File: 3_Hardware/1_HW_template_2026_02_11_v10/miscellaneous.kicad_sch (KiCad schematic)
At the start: 15 parts, among them Q1 BSS316N, SW1 ${SIM.PARAMS}, Y2 ${SIM.PARAMS}

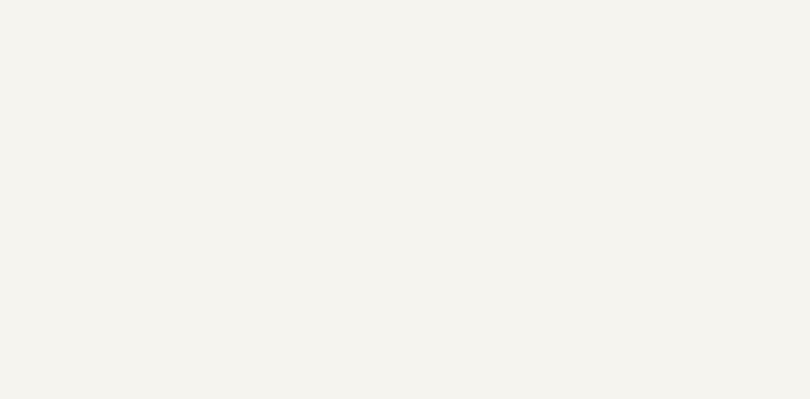
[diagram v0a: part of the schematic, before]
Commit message: first analog circuitry implemented in kicad
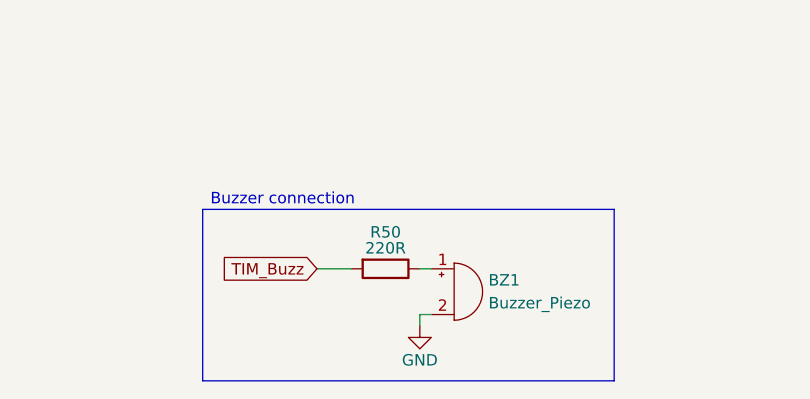
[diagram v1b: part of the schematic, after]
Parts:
- added BZ1: Buzzer_Piezo, Buzzer_Beeper:Buzzer_Murata_PKMCS0909E, symbol Device:Buzzer
- added R50: 220R, Resistor_SMD:R_0805_2012Metric_Pad1.20x1.40mm_HandSolder, symbol Device:R
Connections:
- net GND: now also BZ1.2 (-)
- new net: BZ1.1 (+), R50.1
- new net TIM_Buzz: R50.2
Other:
- note added: "Buzzer connection"

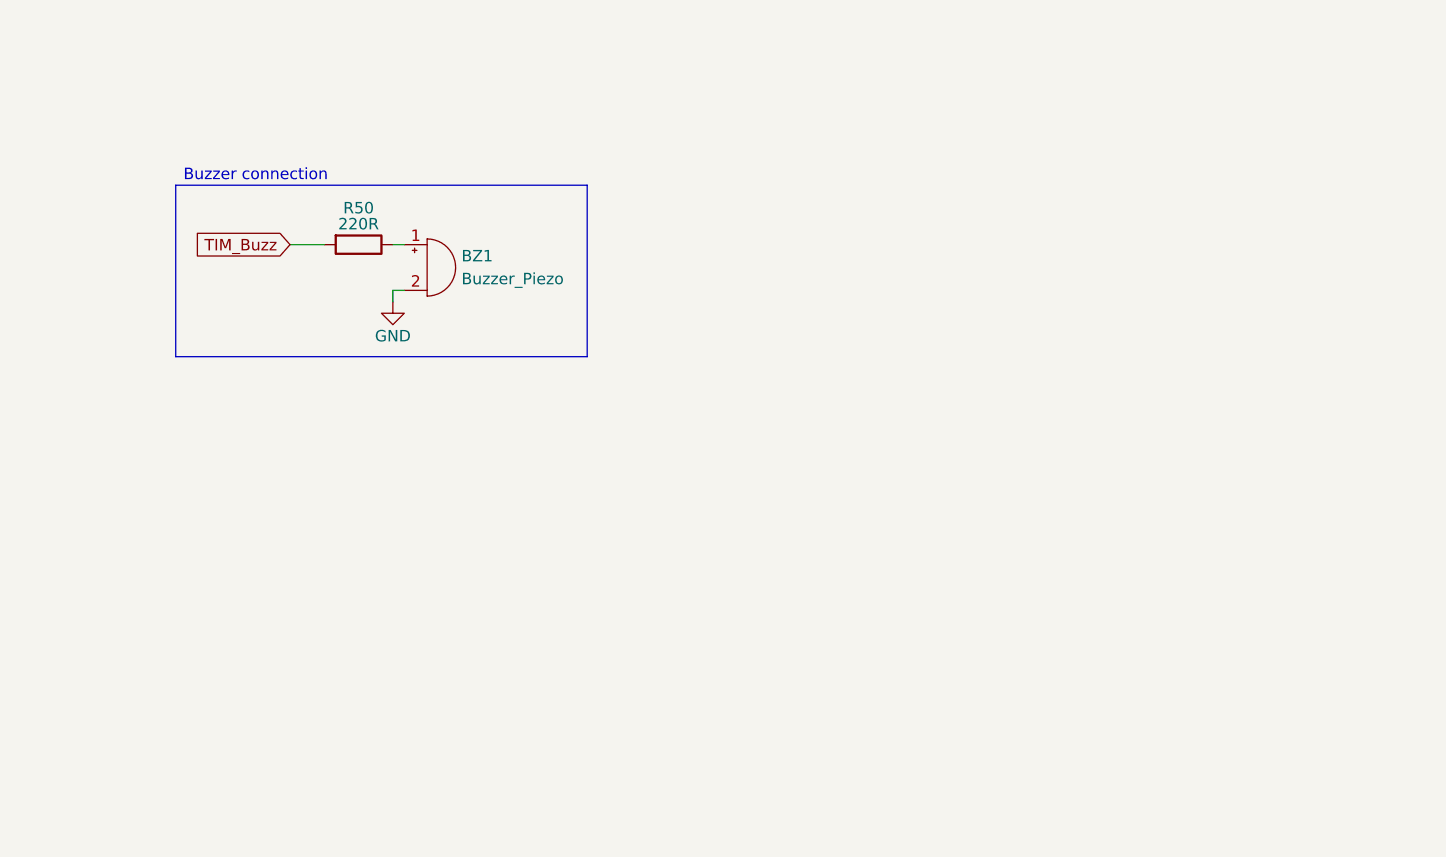
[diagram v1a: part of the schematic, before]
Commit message: finalize main feature
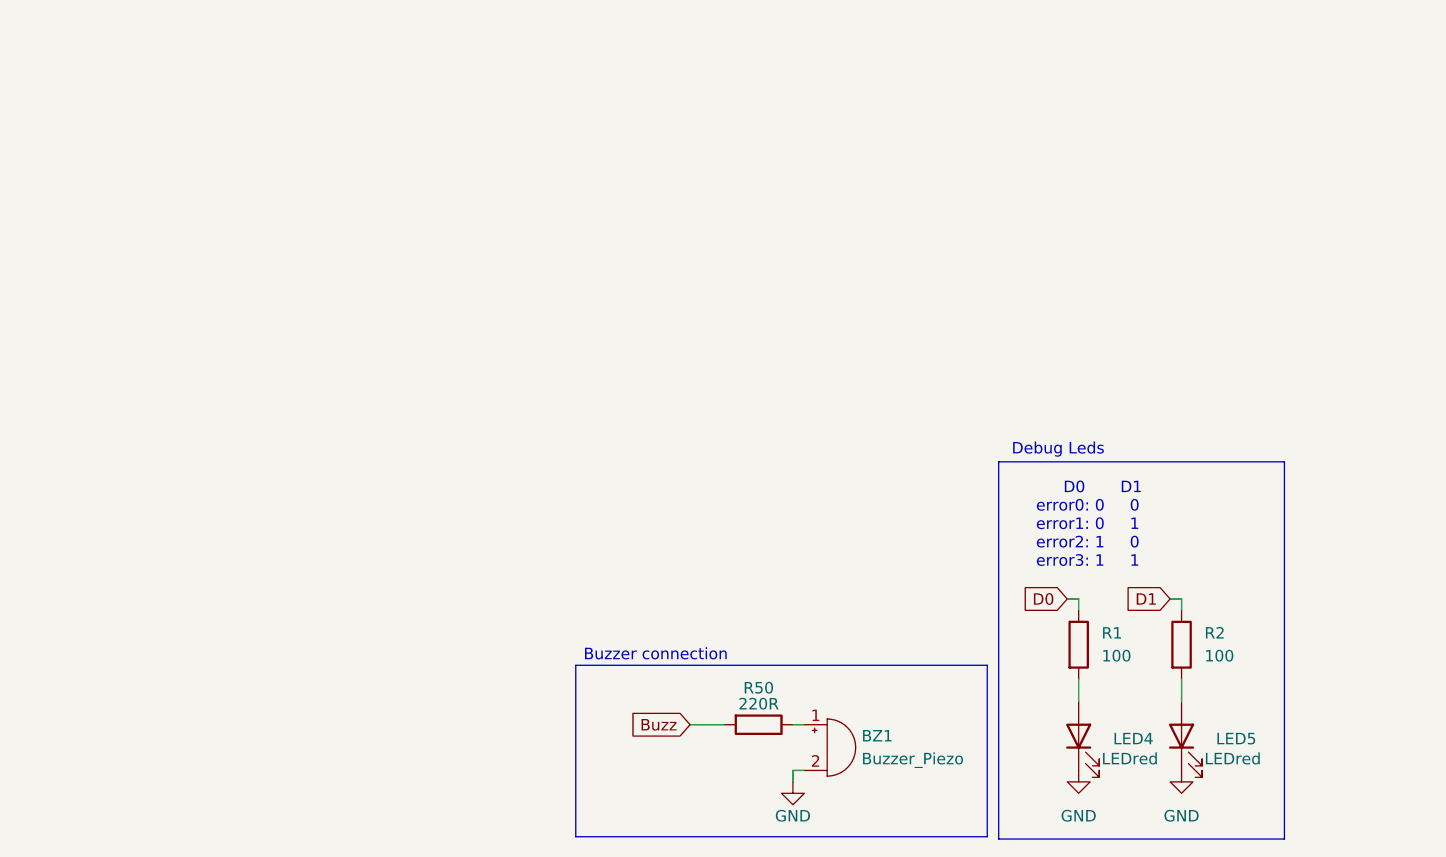
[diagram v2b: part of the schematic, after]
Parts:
- added LED4, LED5: LEDred, LED_SMD:LED_1206_3216Metric_Pad1.42x1.75mm_HandSolder, symbol Device:LED
- added R1, R2: 100, Resistor_SMD:R_0805_2012Metric_Pad1.20x1.40mm_HandSolder, symbol Device:R
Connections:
- net GND: now also LED4.1 (K), LED5.1 (K)
- net TIM_Buzz renamed Buzz
- new net: LED4.2 (A), R1.2
- new net: LED5.2 (A), R2.2
- new net D0: R1.1
- new net D1: R2.1
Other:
- note added: "D0 D1 error0: 0 0 error1: 0 1 error2: 1 0 error3: 1 1"
- note added: "Debug Leds"
- moved on the sheet: BZ1, R50

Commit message: layout template
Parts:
- removed LED1: LEDblue, LED_SMD:LED_1206_3216Metric_Pad1.42x1.75mm_HandSolder, symbol Device:LED
- removed LED2: LEDgreen, LED_SMD:LED_1206_3216Metric_Pad1.42x1.75mm_HandSolder, symbol Device:LED
- removed LED3: LEDred, LED_SMD:LED_1206_3216Metric_Pad1.42x1.75mm_HandSolder, symbol Device:LED
- removed Q1: BSS316N, Package_TO_SOT_SMD:SOT-23, symbol Transistor_FET:BSS138
- removed R16: 22, Resistor_SMD:R_0805_2012Metric_Pad1.20x1.40mm_HandSolder, symbol Device:R
- removed R17: 47, Resistor_SMD:R_0805_2012Metric_Pad1.20x1.40mm_HandSolder, symbol Device:R
- removed R18, R19, R20: 100, Resistor_SMD:R_0805_2012Metric_Pad1.20x1.40mm_HandSolder, symbol Device:R
- removed R21: 10, Resistor_SMD:R_0805_2012Metric_Pad1.20x1.40mm_HandSolder, symbol Device:R
- removed R22: 100k, Resistor_SMD:R_0805_2012Metric_Pad1.20x1.40mm_HandSolder, symbol Device:R
- removed SD1: SD103AWS, Diode_SMD:D_SOD-323_HandSoldering, symbol Device:D_Schottky
- removed SD2: SS13L, Diode_SMD:D_SMA, symbol Device:D_Schottky
- removed SW1: ${SIM.PARAMS}, Button_Switch_SMD:SW_SPST_PTS645, symbol Switch:SW_Push
- LED1: renamed from LED4; footprint LED_SMD:LED_1206_3216Metric_Pad1.42x1.75mm_HandSolder -> LED_SMD:LED_0603_1608Metric_Pad1.05x0.95mm_HandSolder
- LED2: renamed from LED5; footprint LED_SMD:LED_1206_3216Metric_Pad1.42x1.75mm_HandSolder -> LED_SMD:LED_0603_1608Metric_Pad1.05x0.95mm_HandSolder
- R16: renamed from R1; value 100 -> 1k; footprint Resistor_SMD:R_0805_2012Metric_Pad1.20x1.40mm_HandSolder -> Resistor_SMD:R_0603_1608Metric_Pad0.98x0.95mm_HandSolder
- R17: renamed from R2; value 100 -> 1k; footprint Resistor_SMD:R_0805_2012Metric_Pad1.20x1.40mm_HandSolder -> Resistor_SMD:R_0603_1608Metric_Pad0.98x0.95mm_HandSolder
- renumbered R50 to R15, Y2 to Y1
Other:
- note added: "Buzzer"
- note added: "D0 D1"
- note added: "The OpenLog extension"
- note added: "error0: 0 0 error1: 0 1 error2: 1 0 error3: 1 1"
- note removed: "Buzzer connection"
- note removed: "D0 D1 error0: 0 0 error1: 0 1 error2: 1 0 error3: 1 1"
- note removed: "LEDs with different colours"
- note removed: "MOSFET for load switching e.g. buzzer or power LED"
- note removed: "Miscellanneous components and subcircuits: Delete what is no used and copy components that are used several times."
- note removed: "Power Schottky"
- note removed: "Signal Schottky"
- note removed: "The OpenLog extension can be used for logging data onto an SD card"
- moved on the sheet: Y1

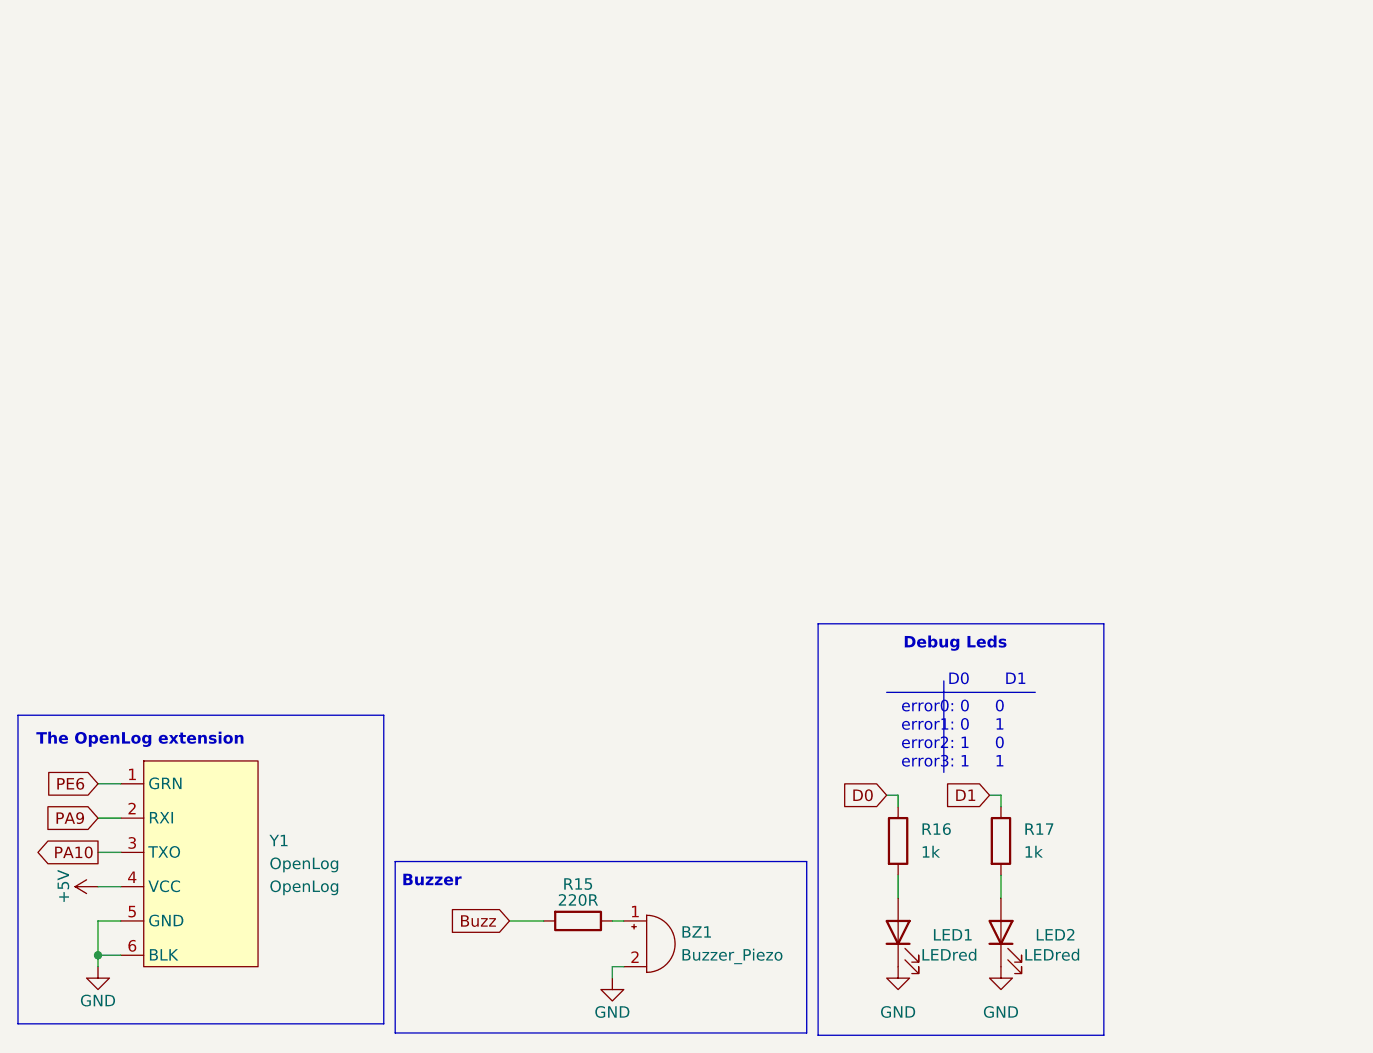
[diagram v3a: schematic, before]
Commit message: updated layout
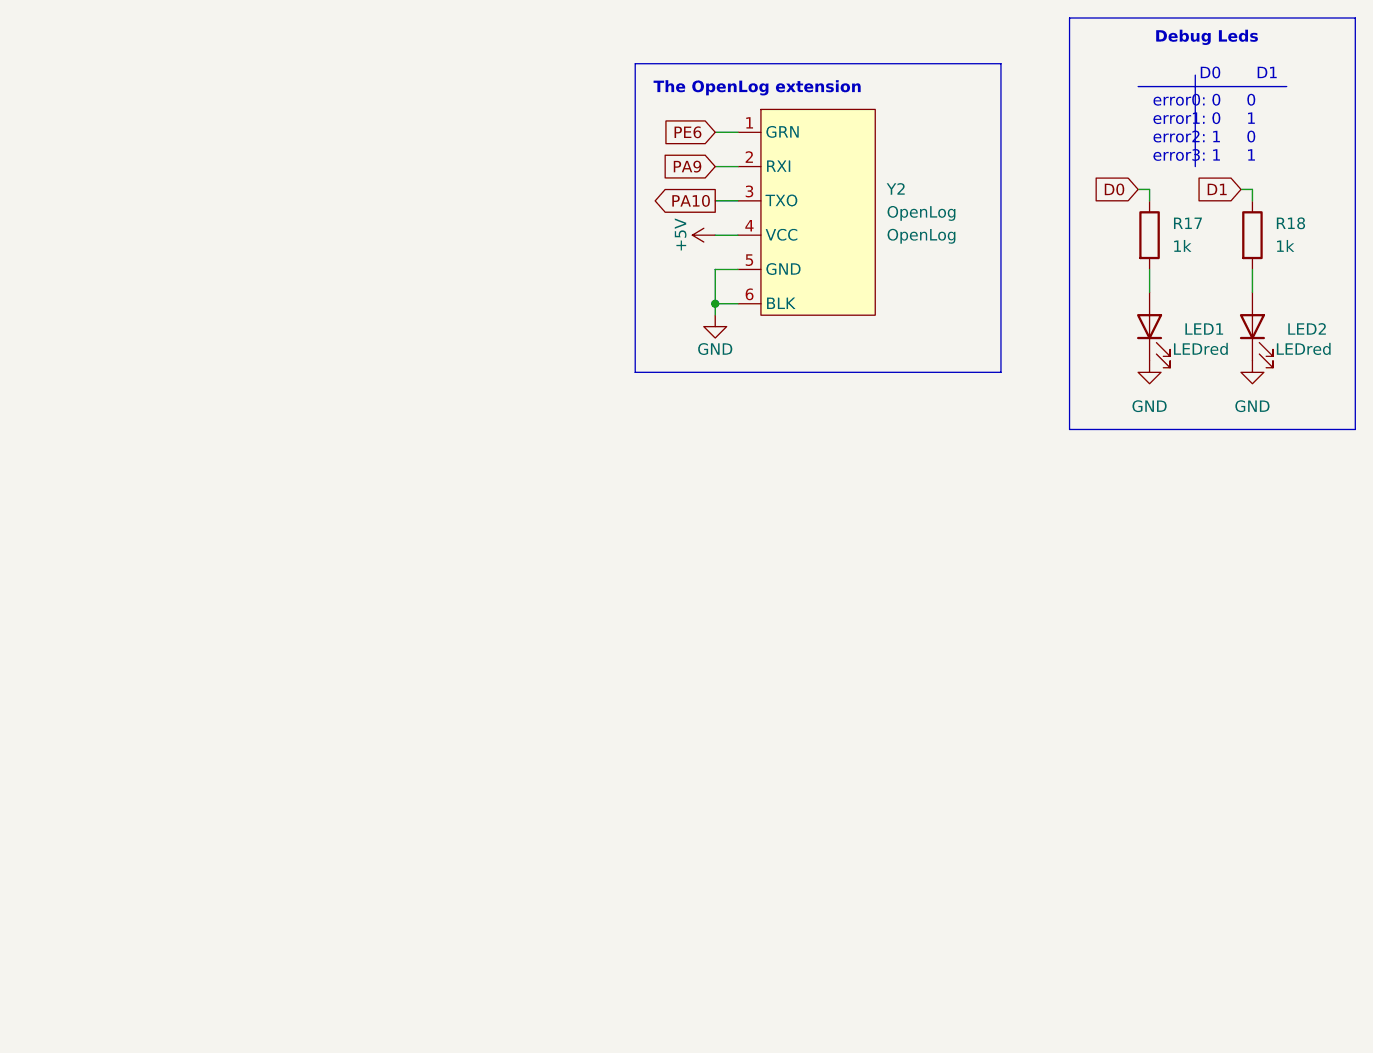
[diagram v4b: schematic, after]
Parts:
- removed BZ1: Buzzer_Piezo, Buzzer_Beeper:Buzzer_Murata_PKMCS0909E, symbol Device:Buzzer
- removed R15: 220R, Resistor_SMD:R_0805_2012Metric_Pad1.20x1.40mm_HandSolder, symbol Device:R
- renumbered R16 to R17, R17 to R18, Y1 to Y2
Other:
- note removed: "Buzzer"
- moved on the sheet: LED1, LED2, R17, R18, Y2

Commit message: pcb schematics finished + layout
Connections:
- net D0 renamed PE5
- net D1 renamed PE3
- net PA10: no longer names the net of Y2.3 (TXO)
- net PA9 renamed PG14_
- net PE6: no longer names the net of Y2.1 (GRN)
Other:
- moved on the sheet: Y2
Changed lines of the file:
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@@
 	(text "The OpenLog extension\n"
 		(exclude_from_sim no)
-		(at 125.222 92.456 0)
+		(at 127.762 92.456 0)
 		(effects
 			(font
@@
 	)
 	(junction
-		(at 132.08 115.57)
+		(at 134.62 115.57)
 		(diameter 0)
 		(color 0 0 0 0)
@@
 	(wire
 		(pts
-			(xy 132.08 111.76) (xy 132.08 115.57)
+			(xy 134.62 111.76) (xy 134.62 115.57)
 		)
 		(stroke
@@
 		)
 	)
-	(wire
-		(pts
-			(xy 132.08 96.52) (xy 134.62 96.52)
-		)
-		(stroke
-			(width 0)
-			(type default)
-		)
-	)
-	(wire
-		(pts
-			(xy 132.08 104.14) (xy 134.62 104.14)
-		)
-		(stroke
-			(width 0)
-			(type default)
-		)
-	)
 	(polyline
 		(pts
@@
 	(wire
 		(pts
-			(xy 132.08 107.95) (xy 134.62 107.95)
+			(xy 134.62 107.95) (xy 137.16 107.95)
 		)
 		(stroke
@@
 	(wire
 		(pts
-			(xy 132.08 115.57) (xy 132.08 116.84)
-		)
-		(stroke
-			(width 0)
-			(type default)
-		)
-	)
-	(wire
-		(pts
-			(xy 134.62 111.76) (xy 132.08 111.76)
-		)
-		(stroke
-			(width 0)
-			(type default)
-		)
-	)
-	(wire
-		(pts
-			(xy 132.08 100.33) (xy 134.62 100.33)
-		)
-		(stroke
-			(width 0)
-			(type default)
-		)
-	)
-	(wire
-		(pts
-			(xy 132.08 115.57) (xy 134.62 115.57)
+			(xy 134.62 115.57) (xy 134.62 116.84)
+		)
+		(stroke
+			(width 0)
+			(type default)
+		)
+	)
+	(wire
+		(pts
+			(xy 137.16 111.76) (xy 134.62 111.76)
+		)
+		(stroke
+			(width 0)
+			(type default)
+		)
+	)
+	(wire
+		(pts
+			(xy 134.62 100.33) (xy 137.16 100.33)
+		)
+		(stroke
+			(width 0)
+			(type default)
+		)
+	)
+	(wire
+		(pts
+			(xy 134.62 115.57) (xy 137.16 115.57)
 		)
 		(stroke
@@
 		)
 	)
-	(global_label "PA9"
+	(global_label "PG14_"
 		(shape input)
-		(at 132.08 100.33 180)
+		(at 134.62 100.33 180)
 		(fields_autoplaced yes)
 		(effects
@@
 		)
 		(property "Intersheetrefs" "${INTERSHEET_REFS}"
-			(at 126.0988 100.2506 0)
+			(at 125.7082 100.33 0)
 			(effects
 				(font
@@
 		)
 	)
-	(global_label "D1"
+	(global_label "PE3"
 		(shape input)
 		(at 190.5 102.87 180)
@@
 		)
 		(property "Intersheetrefs" "${INTERSHEET_REFS}"
-			(at 185.0353 102.87 0)
+			(at 183.8863 102.87 0)
 			(effects
 				(font
@@
 		)
 	)
-	(global_label "PE6"
-		(shape input)
-		(at 132.08 96.52 180)
-		(fields_autoplaced yes)
-		(effects
-			(font
-				(size 1.27 1.27)
-			)
-			(justify right)
-		)
-		(property "Intersheetrefs" "${INTERSHEET_REFS}"
-			(at 126.0383 96.4406 0)
-			(effects
-				(font
-					(size 1.27 1.27)
-				)
-				(justify right)
-				(hide yes)
-			)
-		)
-	)
-	(global_label "D0"
+	(global_label "PE5"
 		(shape input)
 		(at 179.07 102.87 180)
@@
 		)
 		(property "Intersheetrefs" "${INTERSHEET_REFS}"
-			(at 173.6053 102.87 0)
-			(effects
-				(font
-					(size 1.27 1.27)
-				)
-				(justify right)
-				(hide yes)
-			)
-		)
-	)
-	(global_label "PA10"
-		(shape output)
-		(at 132.08 104.14 180)
-		(fields_autoplaced yes)
-		(effects
-			(font
-				(size 1.27 1.27)
-			)
-			(justify right)
-		)
-		(property "Intersheetrefs" "${INTERSHEET_REFS}"
-			(at 124.8893 104.0606 0)
+			(at 172.4563 102.87 0)
 			(effects
 				(font
@@
 	(symbol
 		(lib_id "power:GND")
-		(at 132.08 116.84 0)
+		(at 134.62 116.84 0)
 		(unit 1)
 		(exclude_from_sim no)
@@
 		(dnp no)
 		(property "Reference" "#PWR027"
-			(at 132.08 123.19 0)
+			(at 134.62 123.19 0)
 			(effects
 				(font
@@
 		)
 		(property "Value" "GND"
-			(at 132.08 120.65 0)
+			(at 134.62 120.65 0)
 			(effects
 				(font
@@
 		)
 		(property "Footprint" ""
-			(at 132.08 116.84 0)
+			(at 134.62 116.84 0)
 			(effects
 				(font
@@
 		)
 		(property "Datasheet" ""
-			(at 132.08 116.84 0)
+			(at 134.62 116.84 0)
 			(effects
 				(font
@@
 		)
 		(property "Description" "Power symbol creates a global label with name \"GND\" , ground"
-			(at 132.08 116.84 0)
+			(at 134.62 116.84 0)
 			(effects
 				(font
@@
 	(symbol
 		(lib_id "HW_template:OpenLog")
-		(at 143.51 105.41 0)
+		(at 146.05 105.41 0)
 		(unit 1)
 		(exclude_from_sim no)
@@
 		(on_board yes)
 		(dnp no)
-		(fields_autoplaced yes)
 		(property "Reference" "Y2"
-			(at 151.13 102.8699 0)
+			(at 153.67 102.8699 0)
 			(effects
 				(font
@@
 		)
 		(property "Value" "${SIM.PARAMS}"
-			(at 151.13 105.4099 0)
+			(at 153.67 105.4099 0)
 			(effects
 				(font
@@
 		)
 		(property "Footprint" "Connector_PinHeader_2.54mm:PinHeader_1x06_P2.54mm_Vertical"
-			(at 147.32 120.65 0)
+			(at 149.86 120.65 0)
 			(effects
 				(font
@@
 		)
 		(property "Datasheet" "https://learn.sparkfun.com/tutorials/openlog-hookup-guide"
-			(at 144.78 123.19 0)
+			(at 147.32 123.19 0)
 			(effects
 				(font
@@
 		)
 		(property "Description" "extension for logging data onto an SD card"
-			(at 143.51 105.41 0)
+			(at 146.05 105.41 0)
 			(effects
 				(font
@@
 		)
 		(property "Sim.Device" "SPICE"
-			(at 143.51 105.41 0)
+			(at 146.05 105.41 0)
 			(effects
 				(font
@@
 		)
 		(property "Sim.Params" "OpenLog"
-			(at 151.13 107.9499 0)
+			(at 153.67 107.9499 0)
 			(effects
 				(font
@@
 				)
 				(justify left)
+				(hide yes)
 			)
 		)
 		(property "Sim.Pins" "1=1 2=2 3=3 4=4 5=5 6=6"
-			(at 143.51 105.41 0)
+			(at 146.05 105.41 0)
 			(effects
 				(font
@@
 	(symbol
 		(lib_id "power:+5V")
-		(at 132.08 107.95 90)
+		(at 134.62 107.95 90)
 		(unit 1)
 		(exclude_from_sim no)
@@
 		(dnp no)
 		(property "Reference" "#PWR026"
-			(at 135.89 107.95 0)
+			(at 138.43 107.95 0)
 			(effects
 				(font
@@
 		)
 		(property "Value" "+5V"
-			(at 128.27 107.95 0)
+			(at 130.81 107.95 0)
 			(effects
 				(font
@@
 		)
 		(property "Footprint" ""
-			(at 132.08 107.95 0)
+			(at 134.62 107.95 0)
 			(effects
 				(font
@@
 		)
 		(property "Datasheet" ""
-			(at 132.08 107.95 0)
+			(at 134.62 107.95 0)
 			(effects
 				(font
@@
 		)
 		(property "Description" "Power symbol creates a global label with name \"+5V\""
-			(at 132.08 107.95 0)
-			(effects
-				(font
+			(at 134.62 107.95 0)
+			(effects
+				(font

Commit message: finalized pcb
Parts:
- Y2: footprint Connector_PinHeader_2.54mm:PinHeader_1x06_P2.54mm_Vertical -> Connector_PinSocket_2.54mm:PinSocket_1x06_P2.54mm_Vertical
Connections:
- no-connect marks 0 -> 2
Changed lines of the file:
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@@
 		(color 0 0 0 0)
+	)
+	(no_connect
+		(at 137.16 96.52)
+	)
+	(no_connect
+		(at 137.16 104.14)
 	)
 	(wire
@@
 			)
 		)
-		(property "Footprint" "Connector_PinHeader_2.54mm:PinHeader_1x06_P2.54mm_Vertical"
+		(property "Footprint" "Connector_PinSocket_2.54mm:PinSocket_1x06_P2.54mm_Vertical"
 			(at 149.86 120.65 0)
 			(effects
